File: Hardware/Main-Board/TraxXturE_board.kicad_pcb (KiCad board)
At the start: 4 copper layers, 76.6 x 57.1 mm, 150 parts, among them J1 Conn_01x06, J10 SIM8060-6-1-14-00-A, J3 MSD-10-C, J4 UFL, J5 UFL, J6 UFL, J7 Conn_01x02, J8 Conn_02x06_Odd_Even, J9 Conn_01x02, K1 A161CS12VDC.64, Q1 3416, Q10 AO3400A, Q2 3416, Q3 MMBT2222A, Q4 MMBT2222A, Q5 MGSF1N02LT1G, Q6 MMBT2222A, Q7 IPD90P03P4L-04-HXY, Q8 CJ3401, Q9 AO3400A, SW1 TL3330AF260QG, U1 SIM7600G, U10 SN65LVDS050IPWRQ1, U11 TPS22810DRV, U2 bq34210-Q1, U3 W25Q128JVS, U4 RP2040, U5 MPU-6050, U6 BQ25601, U7 TPS63000, U8 DS3231MZ, U9 SN65LVDS1DBV, Y1 ABM8-272-T3

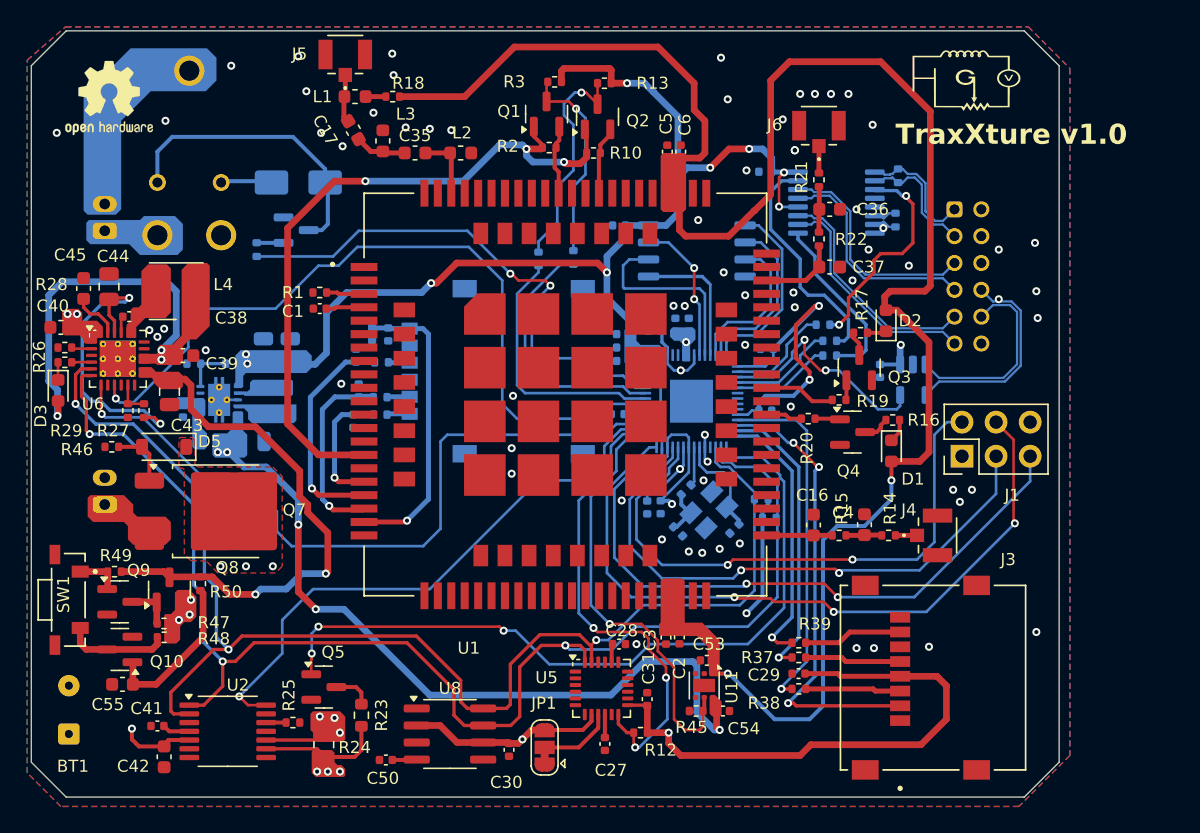
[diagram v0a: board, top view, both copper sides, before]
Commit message: Done with main board design, and camera interconnect in progress
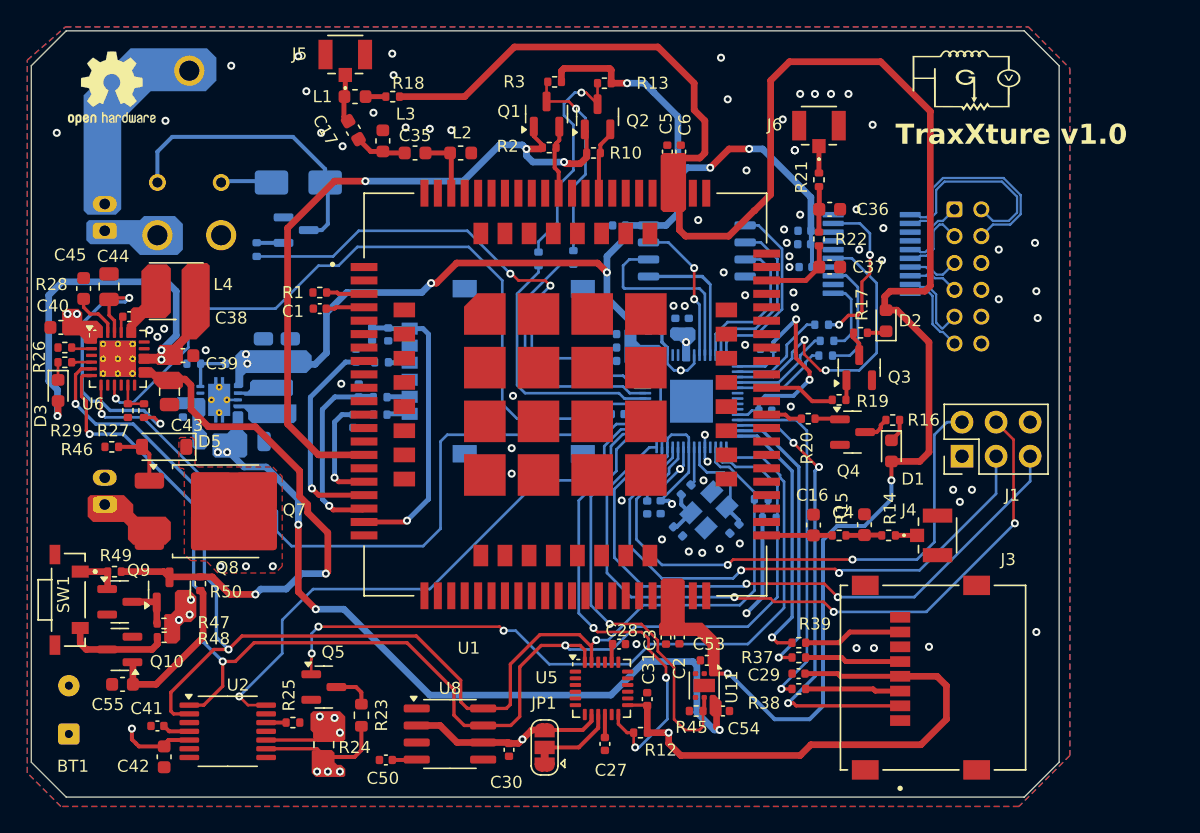
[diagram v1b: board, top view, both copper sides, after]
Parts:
- removed R43, R44: 100R, Resistor_SMD:R_0402_1005Metric
- removed U10: SN65LVDS050IPWRQ1, Package_SO:TSSOP-16_4.4x5mm_P0.65mm
- added C56: 20pF C0G 16V, Capacitor_SMD:C_0402_1005Metric, B.Cu at (155.5, 57.0)
- C51, C52: value 100nF X7R 16V -> 20pF C0G 16V
- R12: value 10k 1% 1/4W -> 10k
- R26: value 470R 1% -> 470R
- R27, R28, R29: value 10k 1% -> 10k
- R30: value 100R 1% -> 100R
- R33, R34: value 10k 1% 1/4W -> 10k 1%
- R9: value 1k 1% 1/4W -> 1k
- U9: value SN65LVDS1DBV -> SN65LVDT41PW; footprint Package_TO_SOT_SMD:SOT-23-5 -> SN65LVDT41PW:SOP65P640X120-20N
- moved C51 11.0 mm to (155.4, 55.3), turned to 0 degrees
- moved U9 9.86 mm to (160.4, 56.0), turned to 0 degrees
- moved C52 5.28 mm to (155.4, 54.3)
- moved REF** 0.73 mm to (103.8, 43.7)
- moved R41 0.30 mm to (157.0, 63.6)
- moved R40 0.20 mm to (157.1, 62.5)
- moved R42 0.10 mm to (156.7, 61.3)
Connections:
- net Net-(U1A-GNSS_ANT) renamed /Architectural_diagram/GSM_GPS_CIRCUITRY/GPS_ANT
- J8 pad 1: /Architectural_diagram/camera_pin_out/CAM_SPI_SDI_D- -> /Architectural_diagram/camera_pin_out/CAM_SPI_CS_D+
- J8 pad 10: /Architectural_diagram/camera_pin_out/CAM_SPI_CS_D- -> GND
- J8 pad 11: /Architectural_diagram/camera_pin_out/CAM_SPI_SDO_D+ -> /Architectural_diagram/camera_pin_out/CAM_SPI_SCK_D+
- J8 pad 12: GND -> +3V3
- J8 pad 2: +3V3 -> /Architectural_diagram/camera_pin_out/CAM_SPI_SDI_D-
- J8 pad 3: /Architectural_diagram/camera_pin_out/CAM_SPI_SDI_D+ -> /Architectural_diagram/camera_pin_out/CAM_SPI_CS_D-
- J8 pad 4: unconnected-(J8-Pin_4-Pad4) -> /Architectural_diagram/camera_pin_out/CAM_SPI_SDI_D+
- J8 pad 5: /Architectural_diagram/camera_pin_out/CAM_SPI_SCK_D+ -> /Architectural_diagram/camera_pin_out/CAM_SPI_SDO_D-
- J8 pad 7: /Architectural_diagram/camera_pin_out/CAM_SPI_SCK_D- -> /Architectural_diagram/camera_pin_out/CAM_SPI_SDO_D+
- J8 pad 8: /Architectural_diagram/camera_pin_out/CAM_SPI_CS_D+ -> unconnected-(J8-Pin_8-Pad8)
- J8 pad 9: /Architectural_diagram/camera_pin_out/CAM_SPI_SDO_D- -> /Architectural_diagram/camera_pin_out/CAM_SPI_SCK_D-
- R40 pad 1: Net-(U10-1D) -> Net-(U9-1D)
- R41 pad 1: Net-(U10-2D) -> Net-(U9-2D)
- R42 pad 1: Net-(U10-1R) -> Net-(U9-5R)
- U9 pad 1: +3V3 -> Net-(U9-1D)
- U9 pad 3: /Architectural_diagram/camera_pin_out/CAM_SPI_CS_D- -> Net-(U9-2D)
- U9 pad 4: /Architectural_diagram/camera_pin_out/CAM_SPI_CS_D+ -> +3V3
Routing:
- net +3V3: track 252.0 -> 230.1 mm, vias 17 -> 14
- net Net-(U10-1D): track 17.3 -> 0.00 mm
- net Net-(U10-1R): track 16.3 -> 0.00 mm, vias 2 -> 0
- net /Architectural_diagram/camera_pin_out/CAM_SPI_SDO_D+: track 17.5 -> 3.89 mm
- net /Architectural_diagram/camera_pin_out/CAM_SPI_SDO_D-: track 17.5 -> 3.89 mm
- net Net-(U10-2D): track 13.2 -> 0.00 mm
- net Net-(U9-5R): track 0.00 -> 12.0 mm, vias 0 -> 2
- net /Architectural_diagram/camera_pin_out/CAM_SPI_SCK_D-: track 16.9 -> 6.24 mm
- net /Architectural_diagram/camera_pin_out/CAM_SPI_SCK_D+: track 16.9 -> 6.24 mm
- net /Architectural_diagram/camera_pin_out/CAM_SPI_CS_D+: track 15.7 -> 5.51 mm
- net /Architectural_diagram/camera_pin_out/CAM_SPI_CS_D-: track 14.8 -> 5.51 mm
- net Net-(U9-2D): track 0.00 -> 8.87 mm
- net /Architectural_diagram/camera_pin_out/CAM_SPI_SDI_D+: track 9.53 -> 16.1 mm
- net /Architectural_diagram/MCU_GPIO/SPI0_CSn: track 17.2 -> 23.1 mm
- net /Architectural_diagram/camera_pin_out/CAM_SPI_SDI_D-: track 9.53 -> 15.2 mm
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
